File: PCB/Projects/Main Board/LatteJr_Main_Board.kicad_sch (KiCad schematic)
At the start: 134 parts, among them IC1 BQ27621YZFR-G1A, J1 Conn_01x04_Pin, J3 USB4056-03-A, J4 Conn_01x04_Pin, J5 Conn_01x04_Pin, J6 Conn_01x02_Socket, P1 RPI-RM2, Q1 BSS138DW, Q2 BSS138DW, SW1 SW_Push, SW2 SW_Push, SW3 SW_Push, SW4 SW_Push, SW5 SW_Push, SW6 SW_Push, SW7 SW_Push, SW8 SW_Push, U1 RP2350_60QFN, U10 HAL4395, U11 HAL4395, U12 HAL4395, U13 HAL4395, U14 HAL4395, U15 HAL4395, U16 HAL4395, U2 HAL4395, U3 HAL4395, U4 TPS63001DRCR, U5 BQ25180, U6 USBLC6-2P6, U7 USBLC6-2P6, U8 USBLC6-2P6, U9 HAL4395, Y1 ABM8-272-T3

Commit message: Some Routing
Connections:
- net +3V3: now also U1.44 (ADC_AVDD), U1.53 (USB_OTP_VDD)
- net D+: no longer R6.1
- net D-: no longer R7.1
- net SAFE_D+: now also R6.1
- net SAFE_D-: now also R7.1
- net at R22.1: now also U1.3 (GPIO1)
- net at R23.1: now also U1.4 (GPIO2)
- net at U1.2 (GPIO0): now also R9.1
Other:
- moved on the sheet: C10, C11, C12, C13, C14, C15, C16, C17, C9, R22, R23, R9

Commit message: Routing
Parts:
- removed R8: 100R, Resistor_SMD:R_0201_0603Metric, symbol Device:R
- removed TP1, TP2, TP3, TP4, TP5: TestPoint, TestPoint:TestPoint_Pad_D1.0mm, symbol Connector:TestPoint
- added SW9: 1TS026A-1000-0550, hhl:1TS026A-1000-0550, symbol hhl:1TS026A-1000-0550
- renumbered TP6 to TP1, TP7 to TP2
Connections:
- net ABXY_EN is gone; now on net BTN_EN: R20.2
- net I2C1_SCL is gone; now on net I2C0_SCL: IC1.A3 (SCL), R4.2, U5.B1 (SCL)
- net I2C1_SDA is gone; now on net I2C0_SDA: IC1.A2 (SDA), R5.1, U5.C1 (SDA)
- net TRIGGER_EN is gone; now on net TRIGGER_EN_R: U15.2 (~{EN}), U16.2 (~{EN})
- net +3V3: now also J4.1 (Pin_1), J5.1 (Pin_1)
- net ADC_0: now also U13.5 (OUT); no longer U15.5 (OUT)
- net ADC_1: now also J5.3 (Pin_3), U14.5 (OUT); no longer U12.5 (OUT)
- net ADC_2: now also J4.3 (Pin_3), U11.5 (OUT), U12.5 (OUT); no longer U10.5 (OUT), U13.5 (OUT)
- net ADC_3: now also U10.5 (OUT), U15.5 (OUT), U3.5 (OUT); no longer U11.5 (OUT), U14.5 (OUT)
- net GND: now also J4.4 (Pin_4), J5.4 (Pin_4), U1.61 (GND), SW9.1, SW9.2
- net TRIGGER_EN_L: now also J5.2 (Pin_2)
- net TRIGGER_EN_R: now also J4.2 (Pin_2)
- net WL_CLK: now also U1.12 (GPIO8)
- net WL_CS: now also U1.10 (GPIO7)
- net WL_D: now also U1.9 (GPIO6)
- net WL_ON: now also U1.8 (GPIO5)
- net at R14.1: now also U1.19 (GPIO15)
- net at R18.1: now also U1.36 (GPIO24)
- net at R15.1: now also U1.18 (GPIO14)
- net at U1.13 (GPIO9): now also R13.1
- net at U1.14 (GPIO10): now also R12.1
- net at U1.15 (GPIO11): now also R21.1
- net I2C0_SDA: now reaches U1.16 (GPIO12)
- net I2C0_SCL: now reaches U1.17 (GPIO13)
- net at U1.28 (GPIO17): now also R11.1
- net at U1.31 (GPIO19): now also R16.1
- net at U1.32 (GPIO20): now also R17.1
- net at U1.35 (GPIO23): now also R19.1
- net at U1.37 (GPIO25): now also R20.1
- net USB_BOOT: now reaches U1.60 (QSPI_SS)
- net USB_BOOT: now also SW9.3, SW9.4
- net at U1.7 (GPIO4): now also R10.1
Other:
- moved on the sheet: R10, R11, R12, R13, R14, R15, R16, R17, R18, R19, R20, R21

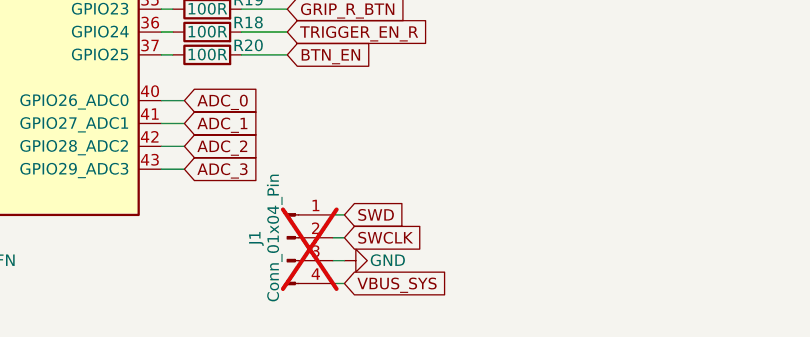
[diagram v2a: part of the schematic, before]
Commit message: Main Board Routing
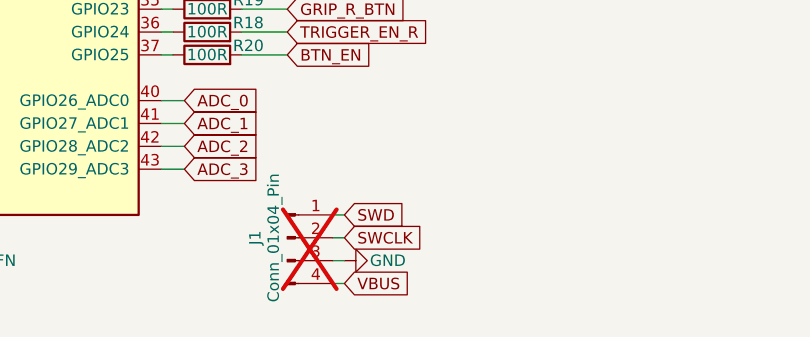
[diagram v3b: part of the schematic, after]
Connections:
- net VBUS: now also J1.4 (Pin_4)
- net VBUS_SYS: no longer J1.4 (Pin_4)
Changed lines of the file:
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@@
 		)
 	)
-	(global_label "VBUS_SYS"
+	(global_label "VBUS"
 		(shape input)
 		(at 157.48 233.68 0)
@@
 		)
 		(property "Intersheetrefs" "${INTERSHEET_REFS}"
-			(at 169.839 233.68 0)
+			(at 165.3638 233.68 0)
 			(effects
 				(font
@@
 		(exclude_from_sim no)
 		(in_bom no)
-		(on_board no)
+		(on_board yes)
 		(dnp yes)
 		(property "Reference" "J1"

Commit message: Prod
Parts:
- J4, J5: LCSC (none) -> C588007; MPN (none) -> 5051100492; Manufacturer (none) -> MOLEX
- J6: LCSC (none) -> C505099; MPN (none) -> 530480210; Manufacturer (none) -> MOLEX
- R30: MPN RC0201FR-07100RL -> RC0201FR-07100RL
- SW9: Manufacturer (none) -> HYP
- U1: LCSC (none) -> C41378174; MPN (none) -> RP2354A; Manufacturer (none) -> Raspberry Pi
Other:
- moved on the sheet: C18, C19, C20, C21, C22, C23, C24, C25, C26, C27, C28, C29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
